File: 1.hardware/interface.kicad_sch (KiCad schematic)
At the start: 36 parts, among them J10 I2C_CONN, J11 ESP_DBG_CONN, J15 CAN_CONN2, J4 UART_CONN, J5 USB_C, J8 ESP_BOOT_CONN, J9 CAN_CONN, U3 SN65HVD230, U4 ESP32-C3-WROOM-02

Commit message: 중간 저장
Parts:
- added J11: EXTRA_SPI3_CONN, Connector_PinSocket_2.54mm:PinSocket_1x06_P2.54mm_Vertical, symbol Connector_Generic:Conn_01x06
- renumbered C57 to C59, C58 to C60, C59 to C61, C60 to C62, C61 to C63, D11 to D10, D9 to D8, D10 to D9, J15 to J10, J8 to J6, J9 to J7, J10 to J8, J11 to J9, R36 to R24, R37 to R25, R38 to R26, R39 to R27, R40 to R28, R41 to R29, R42 to R30, R43 to R31, R44 to R32, R45 to R33, R46 to R34, R47 to R35, R48 to R36, R49 to R37, S3 to S5, U3 to U4, U4 to U5
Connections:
- net +3.3V: no longer J8.1 (Pin_1)
- net GND: now also J11.6 (Pin_6)
- new net 3V3: J11.1 (Pin_1), J8.1 (Pin_1)
- new net EXTRA_SPI3_MISO: J11.3 (Pin_3)
- new net EXTRA_SPI3_MOSI: J11.4 (Pin_4)
- new net EXTRA_SPI3_NSS: J11.5 (Pin_5)
- new net EXTRA_SPI3_SCK: J11.2 (Pin_2)

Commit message: 중간 저장
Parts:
- removed LED3: LED_0603_Green_PWR, PCM_LED_SMD_AKL:LED_0603_1608Metric, symbol PCM_LED_AKL:LED_0603_Green
- removed R24: 4.7k/0.063w, Resistor_SMD:R_0402_1005Metric, symbol Device:R_Small_US
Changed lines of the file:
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@@
 	)
 	(junction
-		(at 62.23 113.03)
-		(diameter 0)
-		(color 0 0 0 0)
-	)
-	(junction
 		(at 127 113.03)
 		(diameter 0)
@@
 	(wire
 		(pts
-			(xy 20.32 113.03) (xy 62.23 113.03)
-		)
-		(stroke
-			(width 0)
-			(type default)
-		)
-	)
-	(wire
-		(pts
 			(xy 171.45 29.21) (xy 177.8 29.21)
 		)
@@
 	(wire
 		(pts
-			(xy 20.32 120.65) (xy 20.32 123.19)
-		)
-		(stroke
-			(width 0)
-			(type default)
-		)
-	)
-	(wire
-		(pts
 			(xy 212.09 36.83) (xy 212.09 40.64)
 		)
@@
 	(wire
 		(pts
-			(xy 20.32 130.81) (xy 20.32 133.35)
-		)
-		(stroke
-			(width 0)
-			(type default)
-		)
-	)
-	(wire
-		(pts
 			(xy 52.07 31.75) (xy 72.39 31.75)
 		)
@@
 	(wire
 		(pts
-			(xy 20.32 113.03) (xy 20.32 115.57)
-		)
-		(stroke
-			(width 0)
-			(type default)
-		)
-	)
-	(wire
-		(pts
 			(xy 173.99 36.83) (xy 171.45 36.83)
 		)
@@
 	)
 	(symbol
-		(lib_id "PCM_LED_AKL:LED_0603_Green")
-		(at 20.32 127 270)
-		(unit 1)
-		(exclude_from_sim no)
-		(in_bom yes)
-		(on_board yes)
-		(dnp no)
-		(property "Reference" "LED3"
-			(at 20.574 124.714 90)
-			(effects
-				(font
-					(size 1.27 1.27)
-				)
-				(justify left)
-			)
-		)
-		(property "Value" "LED_0603_Green_PWR"
-			(at 21.59 130.81 90)
-			(effects
-				(font
-					(size 1.27 1.27)
-				)
-				(justify left)
-			)
-		)
-		(property "Footprint" "PCM_LED_SMD_AKL:LED_0603_1608Metric"
-			(at 20.32 127 0)
-			(effects
-				(font
-					(size 1.27 1.27)
-				)
-				(hide yes)
-			)
-		)
-		(property "Datasheet" "~"
-			(at 20.32 127 0)
-			(effects
-				(font
-					(size 1.27 1.27)
-				)
-				(hide yes)
-			)
-		)
-		(property "Description" "Green SMD LED, 0603, Alternate KiCad Library"
-			(at 20.32 127 0)
-			(effects
-				(font
-					(size 1.27 1.27)
-				)
-				(hide yes)
-			)
-		)
-		(pin "2"
-		)
-		(pin "1"
-		)
-		(instances
-			(project "bldc_motor_controller"
-				(path "/a25adab6-a8c3-4e0e-8ba9-baac00aaa394/430b6e73-4ab5-4f88-adfd-520e070c0b15"
-					(reference "LED3")
-					(unit 1)
-				)
-			)
-		)
-	)
-	(symbol
 		(lib_id "USB-C-USB-2.0-cache:Connector_USB_C_Receptacle_USB2.0")
 		(at 34.29 41.91 0)
@@
 	)
 	(symbol
-		(lib_id "Device:R_Small_US")
-		(at 20.32 118.11 0)
-		(unit 1)
-		(exclude_from_sim no)
-		(in_bom yes)
-		(on_board yes)
-		(dnp no)
-		(property "Reference" "R24"
-			(at 23.368 116.586 0)
-			(effects
-				(font
-					(size 1.27 1.27)
-				)
-			)
-		)
-		(property "Value" "4.7k/0.063w"
-			(at 27.432 120.142 0)
-			(effects
-				(font
-					(size 1.27 1.27)
-				)
-			)
-		)
-		(property "Footprint" "Resistor_SMD:R_0402_1005Metric"
-			(at 20.32 118.11 0)
-			(effects
-				(font
-					(size 1.27 1.27)
-				)
-				(hide yes)
-			)
-		)
-		(property "Datasheet" "~"
-			(at 20.32 118.11 0)
-			(effects
-				(font
-					(size 1.27 1.27)
-				)
-				(hide yes)
-			)
-		)
-		(property "Description" "Resistor, small US symbol"
-			(at 20.32 118.11 0)
-			(effects
-				(font
-					(size 1.27 1.27)
-				)
-				(hide yes)
-			)
-		)
-		(pin "2"
-		)
-		(pin "1"
-		)
-		(instances
-			(project "bldc_motor_controller"
-				(path "/a25adab6-a8c3-4e0e-8ba9-baac00aaa394/430b6e73-4ab5-4f88-adfd-520e070c0b15"
-					(reference "R24")
-					(unit 1)
-				)
-			)
-		)
-	)
-	(symbol
 		(lib_id "Connector_Generic:Conn_01x03")
 		(at 171.45 127 0)
@@
 					(unit 1)
 				)
-			)
-		)
-	)
-	(symbol
-		(lib_id "power:GND")
-		(at 20.32 133.35 0)
-		(unit 1)
-		(exclude_from_sim no)
-		(in_bom yes)
-		(on_board yes)
-		(dnp no)
-		(property "Reference" "#PWR078"
-			(at 20.32 139.7 0)
-			(effects
-				(font
-					(size 1.27 1.27)
-				)
-				(hide yes)
-			)
-		)
-		(property "Value" "GND"
-			(at 20.574 137.922 0)
-			(effects
-				(font
-					(size 1.27 1.27)
-				)
-			)
-		)
-		(property "Footprint" ""
-			(at 20.32 133.35 0)
-			(effects
-				(font
-					(size 1.27 1.27)
-				)
-				(hide yes)
-			)
-		)
-		(property "Datasheet" ""
-			(at 20.32 133.35 0)
-			(effects
-				(font
-					(size 1.27 1.27)
-				)
-				(hide yes)
-			)
-		)
-		(property "Description" "Power symbol creates a global label with name \"GND\" , ground"
-			(at 20.32 133.35 0)
-			(effects
-				(font
-					(size 1.27 1.27)
-				)
-				(hide yes)
-			)
-		)
-		(pin "1"
-		)
-		(instances
-			(project "bldc_motor_controller"
-				(path "/a25adab6-a8c3-4e0e-8ba9-baac00aaa394/430b6e73-4ab5-4f88-adfd-520e070c0b15"
-					(reference "#PWR078")
-					(unit 1)
-				)

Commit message: 중간 저장
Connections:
- net PWR_INPUT(5V~24V) renamed PWR_INPUT(12V~48V)
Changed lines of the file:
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@@
 		)
 	)
-	(global_label "PWR_INPUT(5V~24V)"
+	(global_label "PWR_INPUT(12V~48V)"
 		(shape passive)
 		(at 215.9 29.21 0)
@@
 		)
 		(property "Intersheetrefs" "${INTERSHEET_REFS}"
-			(at 236.6425 29.21 0)
+			(at 237.852 29.21 0)
 			(effects
 				(font
@@
 		)
 	)
-	(global_label "PWR_INPUT(5V~24V)"
+	(global_label "3V3_ESP32"
+		(shape passive)
+		(at 218.44 113.03 0)
+		(fields_autoplaced yes)
+		(effects
+			(font
+				(size 1.27 1.27)
+			)
+			(justify left)
+		)
+		(property "Intersheetrefs" "${INTERSHEET_REFS}"
+			(at 230.8366 113.03 0)
+			(effects
+				(font
+					(size 1.27 1.27)
+				)
+				(justify left)
+				(hide yes)
+			)
+		)
+	)
+	(global_label "ESP_EN"
+		(shape passive)
+		(at 106.68 124.46 180)
+		(fields_autoplaced yes)
+		(effects
+			(font
+				(size 1.27 1.27)
+			)
+			(justify right)
+		)
+		(property "Intersheetrefs" "${INTERSHEET_REFS}"
+			(at 97.7305 124.46 0)
+			(effects
+				(font
+					(size 1.27 1.27)
+				)
+				(justify right)
+				(hide yes)
+			)
+		)
+	)
+	(global_label "UART1_TX"
+		(shape passive)
+		(at 53.34 90.17 0)
+		(fields_autoplaced yes)
+		(effects
+			(font
+				(size 1.27 1.27)
+			)
+			(justify left)
+		)
+		(property "Intersheetrefs" "${INTERSHEET_REFS}"
+			(at 64.2248 90.17 0)
+			(effects
+				(font
+					(size 1.27 1.27)
+				)
+				(justify left)
+				(hide yes)
+			)
+		)
+	)
+	(global_label "ESP32_UART_TX"
+		(shape passive)
+		(at 106.68 132.08 180)
+		(fields_autoplaced yes)
+		(effects
+			(font
+				(size 1.27 1.27)
+			)
+			(justify right)
+		)
+		(property "Intersheetrefs" "${INTERSHEET_REFS}"
+			(at 89.9896 132.08 0)
+			(effects
+				(font
+					(size 1.27 1.27)
+				)
+				(justify right)
+				(hide yes)
+			)
+		)
+	)
+	(global_label "FSPIQ"
+		(shape passive)
+		(at 152.4 144.78 180)
+		(fields_autoplaced yes)
+		(effects
+			(font
+				(size 1.27 1.27)
+			)
+			(justify right)
+		)
+		(property "Intersheetrefs" "${INTERSHEET_REFS}"
+			(at 145.0227 144.78 0)
+			(effects
+				(font
+					(size 1.27 1.27)
+				)
+				(justify right)
+				(hide yes)
+			)
+		)
+	)
+	(global_label "FSPICSO"
+		(shape passive)
+		(at 106.68 154.94 180)
+		(fields_autoplaced yes)
+		(effects
+			(font
+				(size 1.27 1.27)
+			)
+			(justify right)
+		)
+		(property "Intersheetrefs" "${INTERSHEET_REFS}"
+			(at 96.8232 154.94 0)
+			(effects
+				(font
+					(size 1.27 1.27)
+				)
+				(justify right)
+				(hide yes)
+			)
+		)
+	)
+	(global_label "3V3"
+		(shape passive)
+		(at 254 26.67 0)
+		(fields_autoplaced yes)
+		(effects
+			(font
+				(size 1.27 1.27)
+			)
+			(justify left)
+		)
+		(property "Intersheetrefs" "${INTERSHEET_REFS}"
+			(at 259.3815 26.67 0)
+			(effects
+				(font
+					(size 1.27 1.27)
+				)
+				(justify left)
+				(hide yes)
+			)
+		)
+	)
+	(global_label "FSPIWP"
+		(shape passive)
+		(at 106.68 142.24 180)
+		(fields_autoplaced yes)
+		(effects
+			(font
+				(size 1.27 1.27)
+			)
+			(justify right)
+		)
+		(property "Intersheetrefs" "${INTERSHEET_REFS}"
+			(at 97.9118 142.24 0)
+			(effects
+				(font
+					(size 1.27 1.27)
+				)
+				(justify right)
+				(hide yes)
+			)
+		)
+	)
+	(global_label "3V3_MCU"
+		(shape passive)
+		(at 54.61 170.18 0)
+		(fields_autoplaced yes)
+		(effects
+			(font
+				(size 1.27 1.27)
+			)
+			(justify left)
+		)
+		(property "Intersheetrefs" "${INTERSHEET_REFS}"
+			(at 65.011 170.18 0)
+			(effects
+				(font
+					(size 1.27 1.27)
+				)
+				(justify left)
+				(hide yes)
+			)
+		)
+	)
+	(global_label "PWR_INPUT(12V~48V)"
 		(shape passive)
 		(at 132.08 25.4 0)
@@
 		)
 		(property "Intersheetrefs" "${INTERSHEET_REFS}"
-			(at 152.8225 25.4 0)
-			(effects
-				(font
-					(size 1.27 1.27)
-				)
-				(justify left)
-				(hide yes)
-			)
-		)
-	)
-	(global_label "3V3_ESP32"
-		(shape passive)
-		(at 218.44 113.03 0)
-		(fields_autoplaced yes)
-		(effects
-			(font
-				(size 1.27 1.27)
-			)
-			(justify left)
-		)
-		(property "Intersheetrefs" "${INTERSHEET_REFS}"
-			(at 230.8366 113.03 0)
-			(effects
-				(font
-					(size 1.27 1.27)
-				)
-				(justify left)
-				(hide yes)
-			)
-		)
-	)
-	(global_label "ESP_EN"
-		(shape passive)
-		(at 106.68 124.46 180)
-		(fields_autoplaced yes)
-		(effects
-			(font
-				(size 1.27 1.27)
-			)
-			(justify right)
-		)
-		(property "Intersheetrefs" "${INTERSHEET_REFS}"
-			(at 97.7305 124.46 0)
-			(effects
-				(font
-					(size 1.27 1.27)
-				)
-				(justify right)
-				(hide yes)
-			)
-		)
-	)
-	(global_label "UART1_TX"
-		(shape passive)
-		(at 53.34 90.17 0)
-		(fields_autoplaced yes)
-		(effects
-			(font
-				(size 1.27 1.27)
-			)
-			(justify left)
-		)
-		(property "Intersheetrefs" "${INTERSHEET_REFS}"
-			(at 64.2248 90.17 0)
-			(effects
-				(font
-					(size 1.27 1.27)
-				)
-				(justify left)
-				(hide yes)
-			)
-		)
-	)
-	(global_label "ESP32_UART_TX"
-		(shape passive)
-		(at 106.68 132.08 180)
-		(fields_autoplaced yes)
-		(effects
-			(font
-				(size 1.27 1.27)
-			)
-			(justify right)
-		)
-		(property "Intersheetrefs" "${INTERSHEET_REFS}"
-			(at 89.9896 132.08 0)
-			(effects
-				(font
-					(size 1.27 1.27)
-				)
-				(justify right)
-				(hide yes)
-			)
-		)
-	)
-	(global_label "FSPIQ"
-		(shape passive)
-		(at 152.4 144.78 180)
-		(fields_autoplaced yes)
-		(effects
-			(font
-				(size 1.27 1.27)
-			)
-			(justify right)
-		)
-		(property "Intersheetrefs" "${INTERSHEET_REFS}"
-			(at 145.0227 144.78 0)
-			(effects
-				(font
-					(size 1.27 1.27)
-				)
-				(justify right)
-				(hide yes)
-			)
-		)
-	)
-	(global_label "FSPICSO"
-		(shape passive)
-		(at 106.68 154.94 180)
-		(fields_autoplaced yes)
-		(effects
-			(font
-				(size 1.27 1.27)
-			)
-			(justify right)
-		)
-		(property "Intersheetrefs" "${INTERSHEET_REFS}"
-			(at 96.8232 154.94 0)
-			(effects
-				(font
-					(size 1.27 1.27)
-				)
-				(justify right)
-				(hide yes)
-			)
-		)
-	)
-	(global_label "3V3"
-		(shape passive)
-		(at 254 26.67 0)
-		(fields_autoplaced yes)
-		(effects
-			(font
-				(size 1.27 1.27)
-			)
-			(justify left)
-		)
-		(property "Intersheetrefs" "${INTERSHEET_REFS}"
-			(at 259.3815 26.67 0)
-			(effects
-				(font
-					(size 1.27 1.27)
-				)
-				(justify left)
-				(hide yes)
-			)
-		)
-	)
-	(global_label "FSPIWP"
-		(shape passive)
-		(at 106.68 142.24 180)
-		(fields_autoplaced yes)
-		(effects
-			(font
-				(size 1.27 1.27)
-			)
-			(justify right)
-		)
-		(property "Intersheetrefs" "${INTERSHEET_REFS}"
-			(at 97.9118 142.24 0)
-			(effects
-				(font
-					(size 1.27 1.27)
-				)
-				(justify right)
-				(hide yes)
-			)
-		)
-	)
-	(global_label "3V3_MCU"
-		(shape passive)
-		(at 54.61 170.18 0)
-		(fields_autoplaced yes)
-		(effects
-			(font
-				(size 1.27 1.27)
-			)
-			(justify left)
-		)
-		(property "Intersheetrefs" "${INTERSHEET_REFS}"
-			(at 65.011 170.18 0)
-			(effects
-				(font
+			(at 154.032 25.4 0)
+			(effects
+				(font

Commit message: 중간 저장
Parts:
- renumbered C61 to C55, C63 to C56, C59 to C57, C60 to C58, C62 to C59, D8 to D7, D9 to D8, D10 to D9, J9 to J10, J6 to J11, J7 to J4, J8 to J5, J10 to J6, J11 to J7, J5 to J8, J4 to J9, LED4 to LED3, LED5 to LED4, R30 to R21, R31 to R22, R34 to R23, R37 to R24, R35 to R27, R36 to R28, R28 to R29, R29 to R30, R32 to R31, R33 to R32, R27 to R33

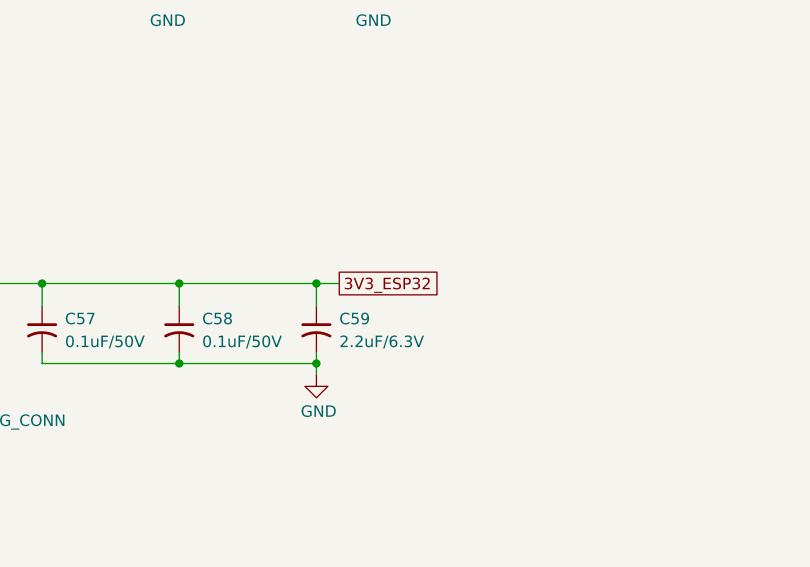
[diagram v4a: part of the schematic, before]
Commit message: 많이 간소화함 일부 핀이 비연결로 확인됨
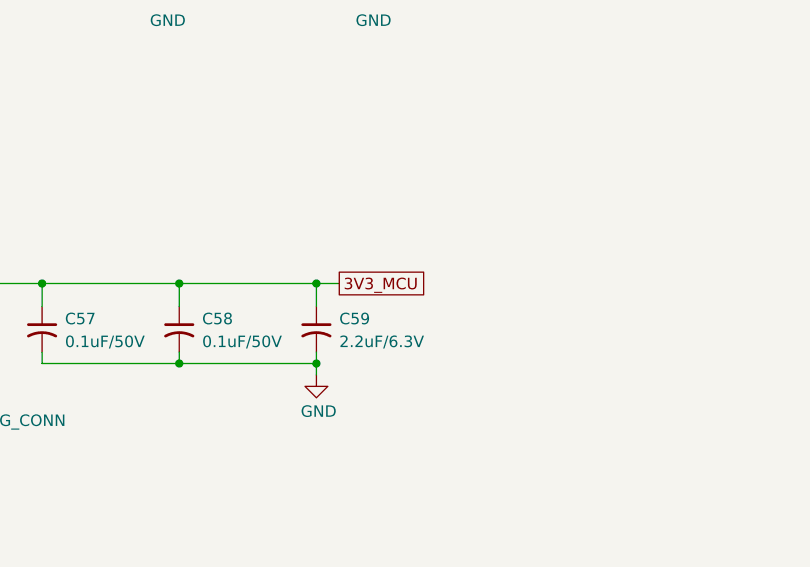
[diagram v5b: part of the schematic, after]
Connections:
- net 3V3_ESP32 is gone; now on net 3V3_MCU: C57.1, C58.1, C59.1, R27.1, R28.1, R29.1, R30.1, U5.1 (3V3)
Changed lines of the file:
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@@
+		)
+	)
+	(global_label "3V3_MCU"
+		(shape passive)
+		(at 218.44 113.03 0)
+		(fields_autoplaced yes)
+		(effects
+			(font
+				(size 1.27 1.27)
+			)
+			(justify left)
+		)
+		(property "Intersheetrefs" "${INTERSHEET_REFS}"
+			(at 228.841 113.03 0)
+			(effects
+				(font
+					(size 1.27 1.27)
+				)
+				(justify left)
+				(hide yes)
+			)
 		)
 	)
@@
 				(hide yes)
 			)
-		)
-	)
-	(global_label "3V3_ESP32"
-		(shape passive)
-		(at 218.44 113.03 0)
-		(fields_autoplaced yes)
-		(effects
-			(font
-				(size 1.27 1.27)
-			)
-			(justify left)
-		)
-		(property "Intersheetrefs" "${INTERSHEET_REFS}"
-			(at 230.8366 113.03 0)
-			(effects
-				(font
-					(size 1.27 1.27)
-				)
-				(justify left)
-				(hide yes)
-			)

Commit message: 중간 저장
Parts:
- added C122: 0.1uF/50V, Capacitor_SMD:C_0603_1608Metric, symbol Device:C_Small_US
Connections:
- net +3.3V is gone; now on net 3V3_MCU: U4.3 (VCC)
- net 3V3_MCU: now also C122.1
- net GND: now also C122.2
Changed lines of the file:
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@@
 	)
 	(junction
+		(at 121.92 53.34)
+		(diameter 0)
+		(color 0 0 0 0)
+	)
+	(junction
 		(at 69.85 113.03)
 		(diameter 0)
@@
 	(wire
 		(pts
+			(xy 134.62 60.96) (xy 134.62 62.23)
+		)
+		(stroke
+			(width 0)
+			(type default)
+		)
+	)
+	(wire
+		(pts
 			(xy 182.88 50.8) (xy 199.39 50.8)
 		)
@@
 	(wire
 		(pts
+			(xy 134.62 53.34) (xy 121.92 53.34)
+		)
+		(stroke
+			(width 0)
+			(type default)
+		)
+	)
+	(wire
+		(pts
 			(xy 49.53 44.45) (xy 52.07 44.45)
 		)
@@
 	(wire
 		(pts
+			(xy 134.62 53.34) (xy 134.62 55.88)
+		)
+		(stroke
+			(width 0)
+			(type default)
+		)
+	)
+	(wire
+		(pts
 			(xy 81.28 40.64) (xy 81.28 60.96)
 		)
@@
 	(wire
 		(pts
-			(xy 121.92 54.61) (xy 121.92 58.42)
+			(xy 203.2 50.8) (xy 203.2 53.34)
 		)
 		(stroke
@@
 	(wire
 		(pts
-			(xy 203.2 50.8) (xy 203.2 53.34)
+			(xy 132.08 68.58) (xy 138.43 68.58)
 		)
 		(stroke
@@
 	(wire
 		(pts
-			(xy 132.08 68.58) (xy 138.43 68.58)
+			(xy 173.99 36.83) (xy 171.45 36.83)
 		)
 		(stroke
@@
 	(wire
 		(pts
-			(xy 173.99 36.83) (xy 171.45 36.83)
+			(xy 119.38 53.34) (xy 121.92 53.34)
 		)
 		(stroke
@@
 	(wire
 		(pts
+			(xy 121.92 53.34) (xy 121.92 58.42)
+		)
+		(stroke
+			(width 0)
+			(type default)
+		)
+	)
+	(wire
+		(pts
 			(xy 248.92 34.29) (xy 254 34.29)
 		)
@@
 		)
 	)
+	(global_label "3V3_MCU"
+		(shape passive)
+		(at 119.38 53.34 180)
+		(fields_autoplaced yes)
+		(effects
+			(font
+				(size 1.27 1.27)
+			)
+			(justify right)
+		)
+		(property "Intersheetrefs" "${INTERSHEET_REFS}"
+			(at 108.979 53.34 0)
+			(effects
+				(font
+					(size 1.27 1.27)
+				)
+				(justify right)
+				(hide yes)
+			)
+		)
+	)
 	(global_label "FSPIWP"
 		(shape passive)
@@
 	)
 	(symbol
+		(lib_id "power:GND")
+		(at 134.62 62.23 0)
+		(unit 1)
+		(exclude_from_sim no)
+		(in_bom yes)
+		(on_board yes)
+		(dnp no)
+		(property "Reference" "#PWR0166"
+			(at 134.62 68.58 0)
+			(effects
+				(font
+					(size 1.27 1.27)
+				)
+				(hide yes)
+			)
+		)
+		(property "Value" "GND"
+			(at 137.668 64.516 0)
+			(effects
+				(font
+					(size 1.27 1.27)
+				)
+			)
+		)
+		(property "Footprint" ""
+			(at 134.62 62.23 0)
+			(effects
+				(font
+					(size 1.27 1.27)
+				)
+				(hide yes)
+			)
+		)
+		(property "Datasheet" ""
+			(at 134.62 62.23 0)
+			(effects
+				(font
+					(size 1.27 1.27)
+				)
+				(hide yes)
+			)
+		)
+		(property "Description" "Power symbol creates a global label with name \"GND\" , ground"
+			(at 134.62 62.23 0)
+			(effects
+				(font
+					(size 1.27 1.27)
+				)
+				(hide yes)
+			)
+		)
+		(pin "1"
+		)
+		(instances
+			(project "bldc_motor_controller"
+				(path "/a25adab6-a8c3-4e0e-8ba9-baac00aaa394/430b6e73-4ab5-4f88-adfd-520e070c0b15"
+					(reference "#PWR0166")
+					(unit 1)
+				)
+			)
+		)
+	)
+	(symbol
 		(lib_id "USB-C-USB-2.0-cache:Connector_USB_C_Receptacle_USB2.0")
 		(at 34.29 41.91 0)
@@
 	)
 	(symbol
-		(lib_id "power:+3.3V")
-		(at 121.92 54.61 0)
-		(unit 1)
-		(exclude_from_sim no)
-		(in_bom yes)
-		(on_board yes)
-		(dnp no)
-		(fields_autoplaced yes)
-		(property "Reference" "#PWR079"
-			(at 121.92 58.42 0)
-			(effects
-				(font
-					(size 1.27 1.27)
-				)
-				(hide yes)
-			)
-		)
-		(property "Value" "+3.3V"
-			(at 121.92 49.53 0)
-			(effects
-				(font
-					(size 1.27 1.27)
-				)
-			)
-		)
-		(property "Footprint" ""
-			(at 121.92 54.61 0)
-			(effects
-				(font
-					(size 1.27 1.27)
-				)
-				(hide yes)
-			)
-		)
-		(property "Datasheet" ""
-			(at 121.92 54.61 0)
-			(effects
-				(font
-					(size 1.27 1.27)
-				)
-				(hide yes)
-			)
-		)
-		(property "Description" "Power symbol creates a global label with name \"+3.3V\""
-			(at 121.92 54.61 0)
-			(effects
-				(font
-					(size 1.27 1.27)
-				)
-				(hide yes)
-			)
-		)
-		(pin "1"
-		)
-		(instances
-			(project "bldc_motor_controller"
-				(path "/a25adab6-a8c3-4e0e-8ba9-baac00aaa394/430b6e73-4ab5-4f88-adfd-520e070c0b15"
-					(reference "#PWR079")
-					(unit 1)
-				)
-			)
-		)
-	)
-	(symbol
 		(lib_id "Device:R_Small_US")
 		(at 36.83 82.55 0)
@@
 	)
 	(symbol
+		(lib_id "Device:C_Small_US")
+		(at 134.62 58.42 0)
+		(unit 1)
+		(exclude_from_sim no)
+		(in_bom yes)
+		(on_board yes)
+		(dnp no)
+		(fields_autoplaced yes)
+		(property "Reference" "C122"
+			(at 137.16 57.2769 0)
+			(effects
+				(font
+					(size 1.27 1.27)
+				)
+				(justify left)
+			)
+		)
+		(property "Value" "0.1uF/50V"
+			(at 137.16 59.8169 0)
+			(effects
+				(font
+					(size 1.27 1.27)
+				)
+				(justify left)
+			)
+		)
+		(property "Footprint" "Capacitor_SMD:C_0603_1608Metric"
+			(at 134.62 58.42 0)
+			(effects
+				(font
+					(size 1.27 1.27)
+				)
+				(hide yes)
+			)
+		)
+		(property "Datasheet" ""
+			(at 134.62 58.42 0)
+			(effects
+				(font
+					(size 1.27 1.27)
+				)
+				(hide yes)
+			)
+		)
+		(property "Description" "capacitor, small US symbol"
+			(at 134.62 58.42 0)
+			(effects
+				(font
+					(size 1.27 1.27)
+				)
+				(hide yes)
+			)
+		)
+		(pin "1"
+		)
+		(pin "2"
+		)
+		(instances
+			(project "bldc_motor_controller"
+				(path "/a25adab6-a8c3-4e0e-8ba9-baac00aaa394/430b6e73-4ab5-4f88-adfd-520e070c0b15"
+					(reference "C122")
+					(unit 1)
+				)
+			)
+		)
+	)
+	(symbol
 		(lib_id "power:GND")
 		(at 121.92 78.74 0)
@@
 		(on_board yes)
 		(dnp no)
-		(fields_autoplaced yes)
 		(property "Reference" "U4"
 			(at 124.0633 55.88 0)
@@
 		)
 		(property "Value" "SN65HVD230"
-			(at 124.0633 58.42 0)
+			(at 122.428 58.166 0)
 			(effects
 				(font
